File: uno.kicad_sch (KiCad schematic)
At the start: 42 parts

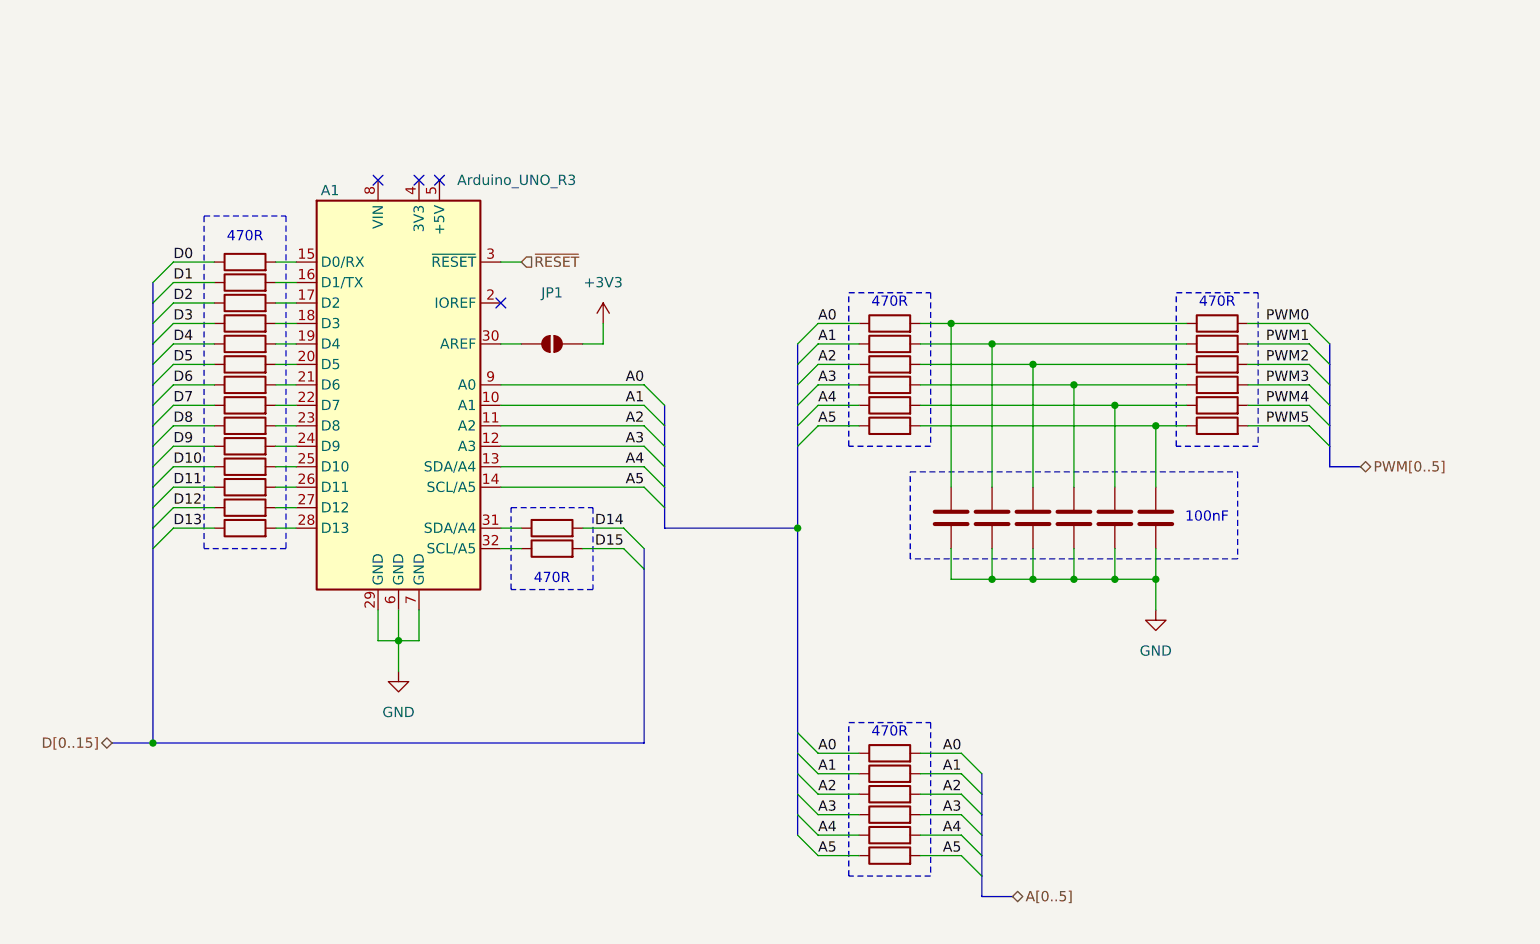
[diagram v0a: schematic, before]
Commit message: Add RP2350B from example
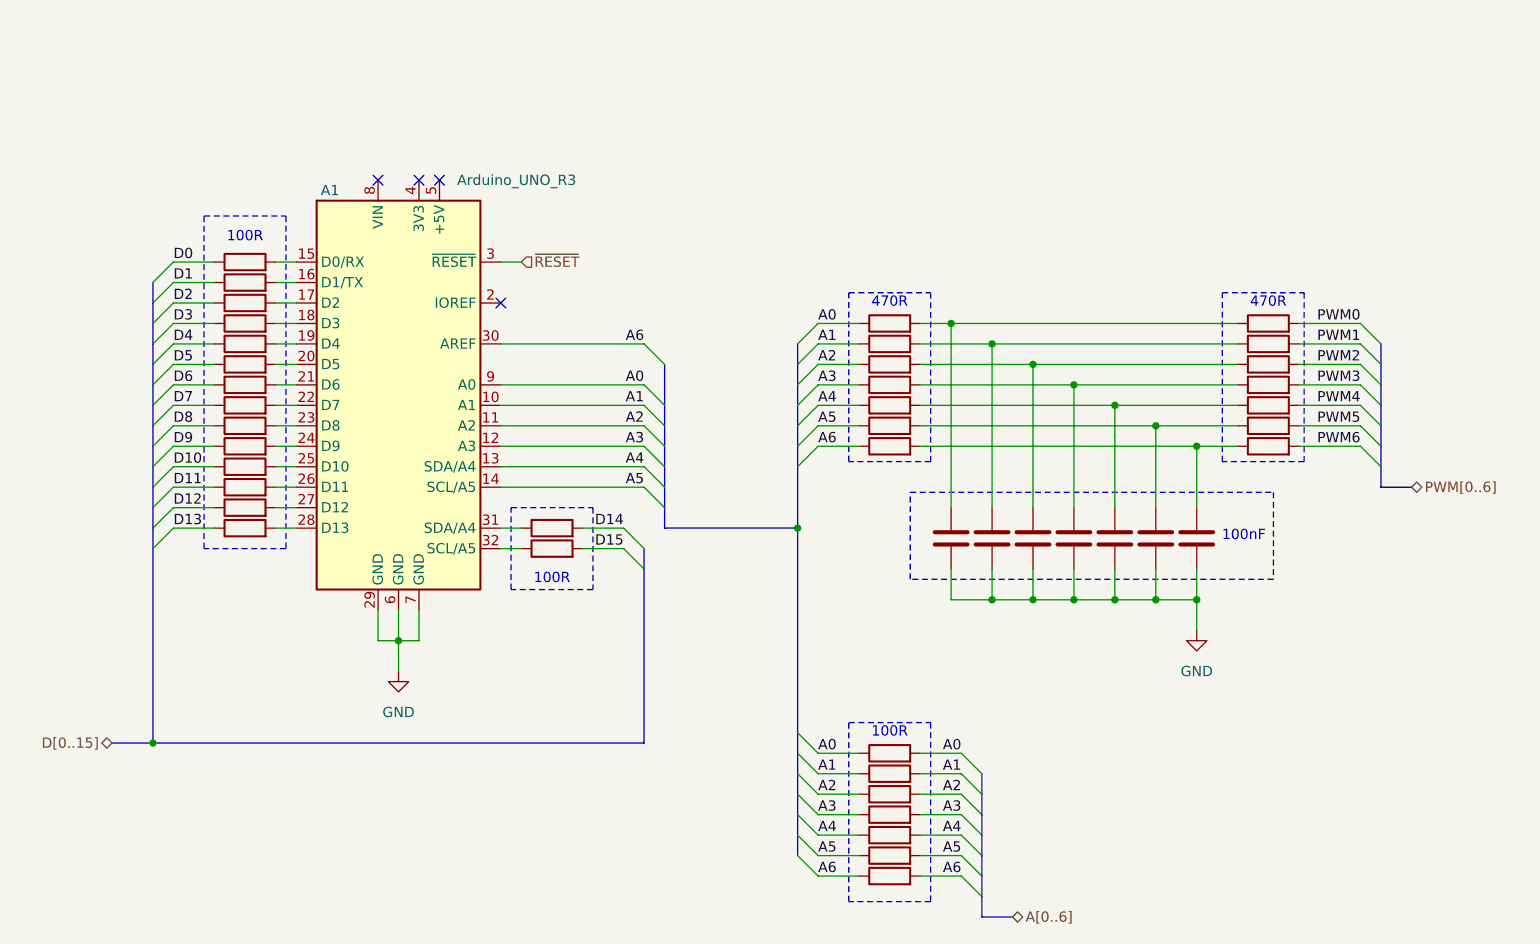
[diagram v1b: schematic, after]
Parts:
- removed JP1: SolderJumper_2_Open, Jumper:SolderJumper-2_P1.3mm_Open_TrianglePad1.0x1.5mm, symbol Jumper:SolderJumper_2_Open
- added C11: 100nF, Capacitor_SMD:C_0402_1005Metric, symbol Device:C
- added R50: 100R, Resistor_SMD:R_0402_1005Metric_Pad0.72x0.64mm_HandSolder, symbol Device:R
- added R51, R52: 470R, Resistor_SMD:R_0402_1005Metric_Pad0.72x0.64mm_HandSolder, symbol Device:R
- A1: now left out of the parts list
- R16, R37, R40, R41, R42, R43, R44, R45, R46, R47, R48, R49: footprint Resistor_SMD:R_0402_1005Metric -> Resistor_SMD:R_0402_1005Metric_Pad0.72x0.64mm_HandSolder
- R17, R18, R19, R20, R21, R22, R23, R24, R25, R26, R27, R28, R29, R30, R31, R32, R33, R34, R35, R36, R38, R39: value 470R -> 100R; footprint Resistor_SMD:R_0402_1005Metric -> Resistor_SMD:R_0402_1005Metric_Pad0.72x0.64mm_HandSolder; LCSC C25117 -> C25076
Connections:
- net GND: now also C11.2
- net A6: now reaches A1.30 (AREF)
- net A6: now also R50.1, R50.2, R51.1
- new net: C11.1, R51.2, R52.1
- new net PWM6: R52.2
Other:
- note added: "100R"

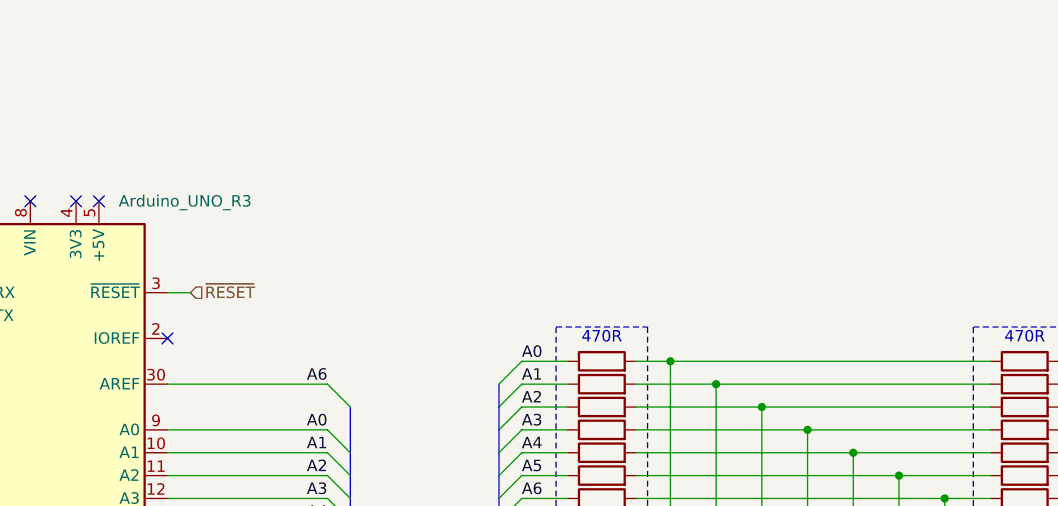
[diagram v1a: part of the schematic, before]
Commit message: Do pin assignment for tester
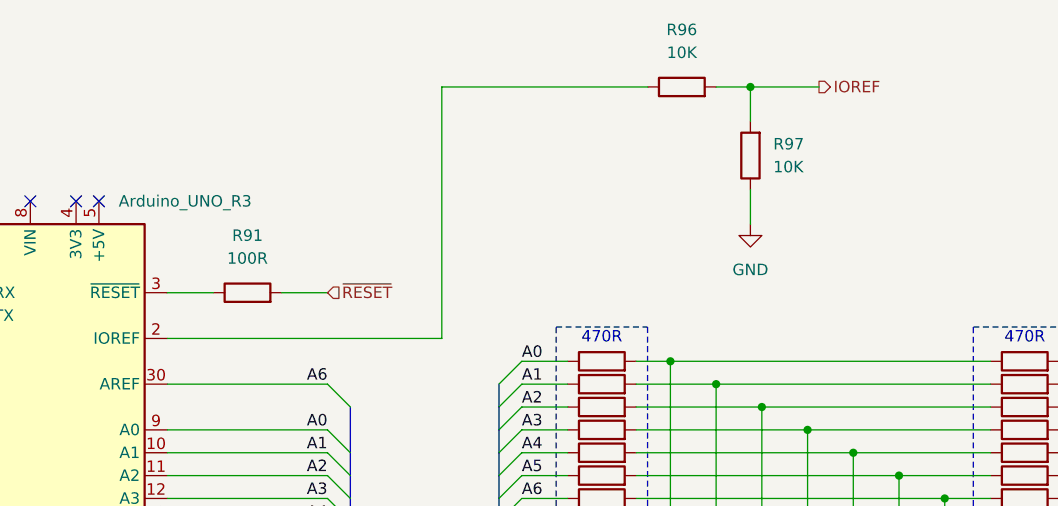
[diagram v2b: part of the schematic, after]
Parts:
- added R91: 100R, Resistor_SMD:R_0402_1005Metric_Pad0.72x0.64mm_HandSolder, symbol Device:R
- added R96, R97: 10K, Resistor_SMD:R_0402_1005Metric_Pad0.72x0.64mm_HandSolder, symbol Device:R
- renumbered R17 to R16, R18 to R17, R19 to R18, R20 to R19, R21 to R20, R22 to R21, R23 to R22, R24 to R23, R25 to R24, R26 to R25, R27 to R26, R28 to R27, R29 to R28, R30 to R29, R38 to R30, R39 to R31, R16 to R32, R37 to R33, R40 to R34, R41 to R35, R42 to R36, R43 to R37, R51 to R38, R31 to R39, R32 to R40, R33 to R41, R34 to R42, R35 to R43, R36 to R44, R50 to R45, R44 to R46, R45 to R47, R46 to R48, R47 to R49, R48 to R50, R49 to R51
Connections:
- net GND: now also R97.1
- net ~{RESET}: now also R91.2; no longer A1.3 (~{RESET})
- net at A1.2 (IOREF): now also R96.1
- new net: A1.3 (~{RESET}), R91.1
- new net IOREF: R96.2, R97.2
- no-connect marks 4 -> 3

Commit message: Start Layout
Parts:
- removed R96, R97: 10K, Resistor_SMD:R_0402_1005Metric_Pad0.72x0.64mm_HandSolder, symbol Device:R
- A1: footprint Module:Arduino_UNO_R3 -> ProjectSpecific:Arduino_UNO_R3_ShieldBase
- C10, C11, C5, C6, C7, C8, C9: footprint Capacitor_SMD:C_0402_1005Metric -> Capacitor_SMD:C_0402_1005Metric_Pad0.74x0.62mm_HandSolder
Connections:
- net A0: no longer A1.9 (A0), R32.1, R39.1
- net A1: no longer A1.10 (A1), R33.1, R40.1
- net A2: no longer A1.11 (A2), R34.1, R41.1
- net A3: no longer A1.12 (A3), R35.1, R42.1
- net A4: no longer A1.13 (SDA/A4), R36.1, R43.1
- net A5: no longer A1.14 (SCL/A5), R37.1, R44.1
- net A6: no longer A1.30 (AREF), R38.1, R45.1
- new net AI0: A1.9 (A0), R32.1, R39.1
- new net AI1: A1.10 (A1), R33.1, R40.1
- new net AI2: A1.11 (A2), R34.1, R41.1
- new net AI3: A1.12 (A3), R35.1, R42.1
- new net AI4: A1.13 (SDA/A4), R36.1, R43.1
- new net AI5: A1.14 (SCL/A5), R37.1, R44.1
- new net AI6: A1.30 (AREF), R38.1, R45.1
- no-connect marks 3 -> 4
